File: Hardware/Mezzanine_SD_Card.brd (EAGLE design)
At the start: 30.5 x 44.5 mm, 11 parts, among them U1 USD-SOCKETNEW, U2 EDISON_CONNECTOR_FULLMOUNTING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, U3 EDISON_CONNECTOR_FULLHEADER

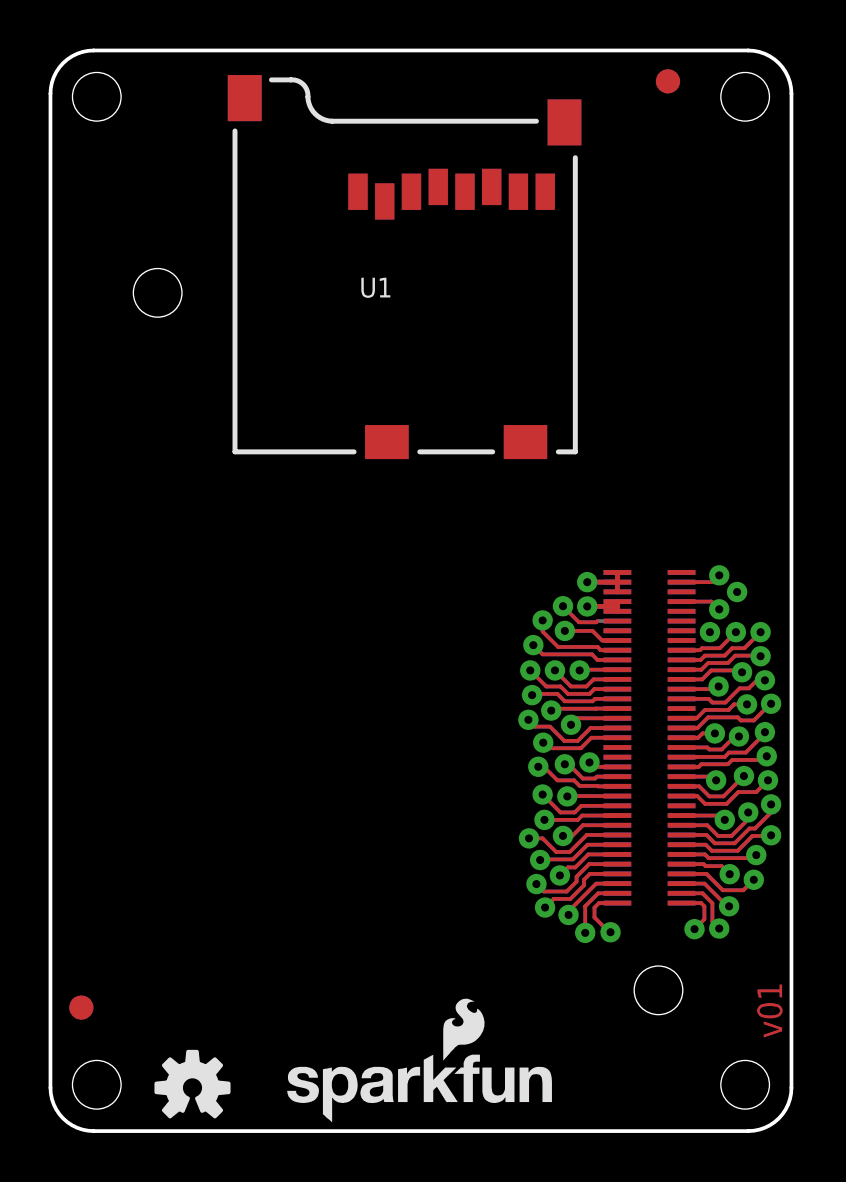
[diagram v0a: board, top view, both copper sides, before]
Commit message: added fiducials
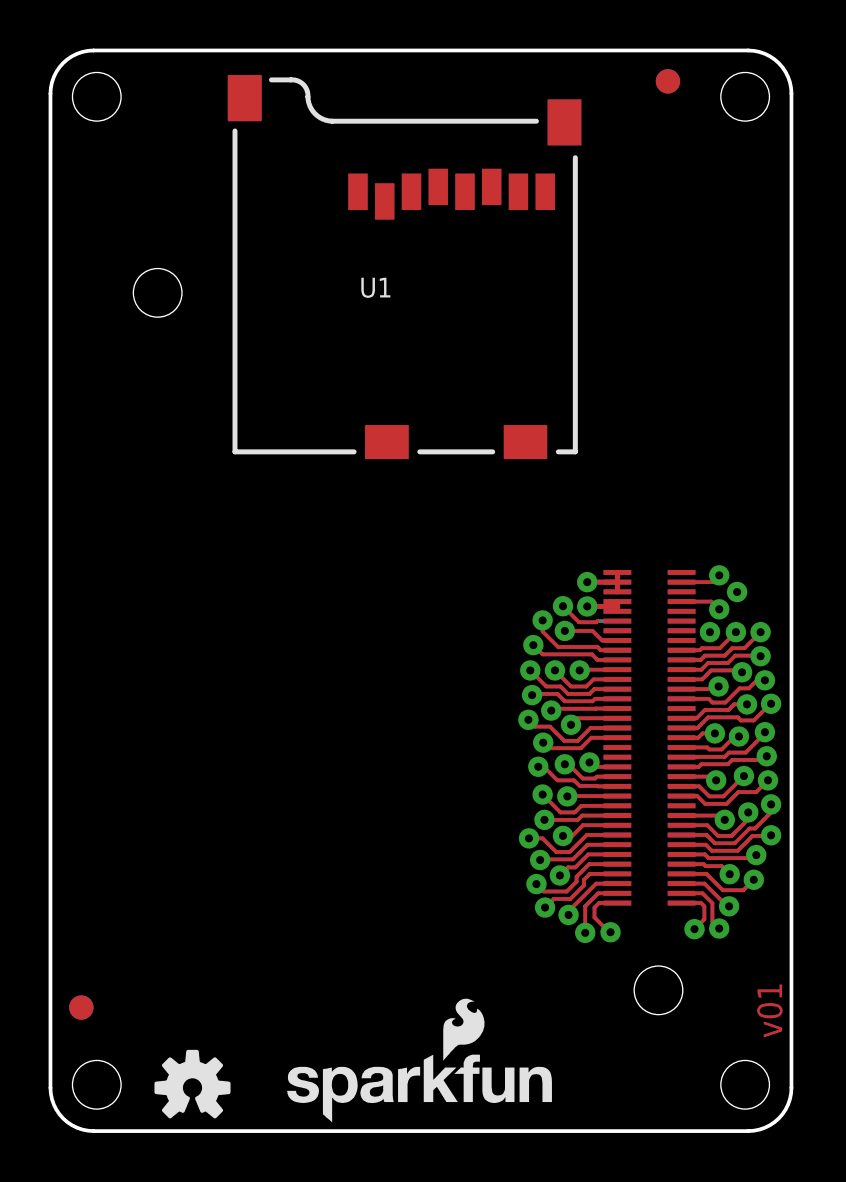
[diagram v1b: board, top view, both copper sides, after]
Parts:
- added FID3, FID4: FIDUCIAL1X2, SparkFun-Aesthetics:FIDUCIAL-1X2
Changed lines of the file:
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@@
 <setting verticaltext="up"/>
 </settings>
-<grid distance="0.4" unitdist="mm" unit="mm" style="lines" multiple="1" display="yes" altdistance="0.005" altunitdist="inch" altunit="inch"/>
+<grid distance="0.01" unitdist="inch" unit="inch" style="lines" multiple="1" display="yes" altdistance="0.005" altunitdist="inch" altunit="inch"/>
 <layers>
 <layer number="1" name="Top" color="4" fill="1" visible="yes" active="yes"/>
@@
 <element name="FID2" library="SparkFun-Aesthetics" package="FIDUCIAL-1X2" value="FIDUCIAL1X2" x="25.4" y="43.18"/>
 <element name="U1" library="SparkFun-Connectors" package="MICRO-SD-SOCKET-PP" value="USD-SOCKETNEW" x="21.59" y="27.94"/>
+<element name="FID3" library="SparkFun-Aesthetics" package="FIDUCIAL-1X2" value="FIDUCIAL1X2" x="1.27" y="5.08" rot="MR0"/>
+<element name="FID4" library="SparkFun-Aesthetics" package="FIDUCIAL-1X2" value="FIDUCIAL1X2" x="25.4" y="43.18" rot="MR0"/>
 </elements>
 <signals>

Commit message: Layout complete, Ready for review.
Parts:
- added C1, C2: 0.1uF, SparkFun-Capacitors:0603-CAP
- added U$1: TXB0108, Testing:UFDFN-20
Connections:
- new net N$1: U$1.P$20, U1.1
- new net N$2: U$1.P$19, U1.2
- new net N$3: U$1.P$18, U1.3
- new net N$4: U$1.P$17, U1.5
- new net N$5: U$1.P$14, U1.7
- new net N$6: U$1.P$13, U1.8
- net 1.8V: now also C1.1, U$1.P$5
- net 3.3V: now also C2.1, U$1.P$16, U1.4
- net GND: now also C1.2, C2.2, U$1.P$15, U$1.P$6, U1.6; no longer U1.CD1
- net GP77_SD_0_CD#: now also U1.CD1
- net GP78_SD_0_CLK: now also U$1.P$4
- net GP79_SD_0_CMD: now also U$1.P$3
- net GP80_SD_0_DAT0: now also U$1.P$7
- net GP81_SD_0_DAT1: now also U$1.P$8
- net GP82_SD_0_DAT2: now also U$1.P$1
- net GP83_SD_0_DAT3: now also U$1.P$2
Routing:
- net 3.3V: track 3.68 -> 36.1 mm, vias 1 -> 4
- net GP83_SD_0_DAT3: track 5.27 -> 31.0 mm, vias 1 -> 2
- net GP81_SD_0_DAT1: track 4.68 -> 29.5 mm, vias 1 -> 3
- net GP80_SD_0_DAT0: track 5.27 -> 29.4 mm, vias 1 -> 2
- net GP82_SD_0_DAT2: track 7.36 -> 28.9 mm
- net GP77_SD_0_CD#: track 5.45 -> 26.2 mm
- net GP79_SD_0_CMD: track 8.08 -> 27.4 mm
- net GP78_SD_0_CLK: track 6.88 -> 25.3 mm
- net 1.8V: track 4.25 -> 20.6 mm, vias 1 -> 3
- net N$6: track 0.00 -> 15.9 mm
- net N$5: track 0.00 -> 15.6 mm
- net N$4: track 0.00 -> 15.2 mm
- net N$3: track 0.00 -> 14.4 mm
- net N$1: track 0.00 -> 13.9 mm
- net N$2: track 0.00 -> 13.8 mm
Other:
- board text added: "Edzzanine uSD"
- board text removed: "Edzzanine SD"
